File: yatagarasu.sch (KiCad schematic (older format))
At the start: 74 parts, among them CON1 CONSOLE, P1 CONN_02X20, P2 +12V_IN, P3 ttyAMA2, Q1 MMBT3904, Q2 MMBT3904, SW1 RESET, U1 8T245, U16 FT230XS, U17 NCP1117ST18T3G, U18 NCP1117ST33T3G, U19 NCP1117ST50T3G, U2 8T245, U3 PCA9306, U4 PCA9306

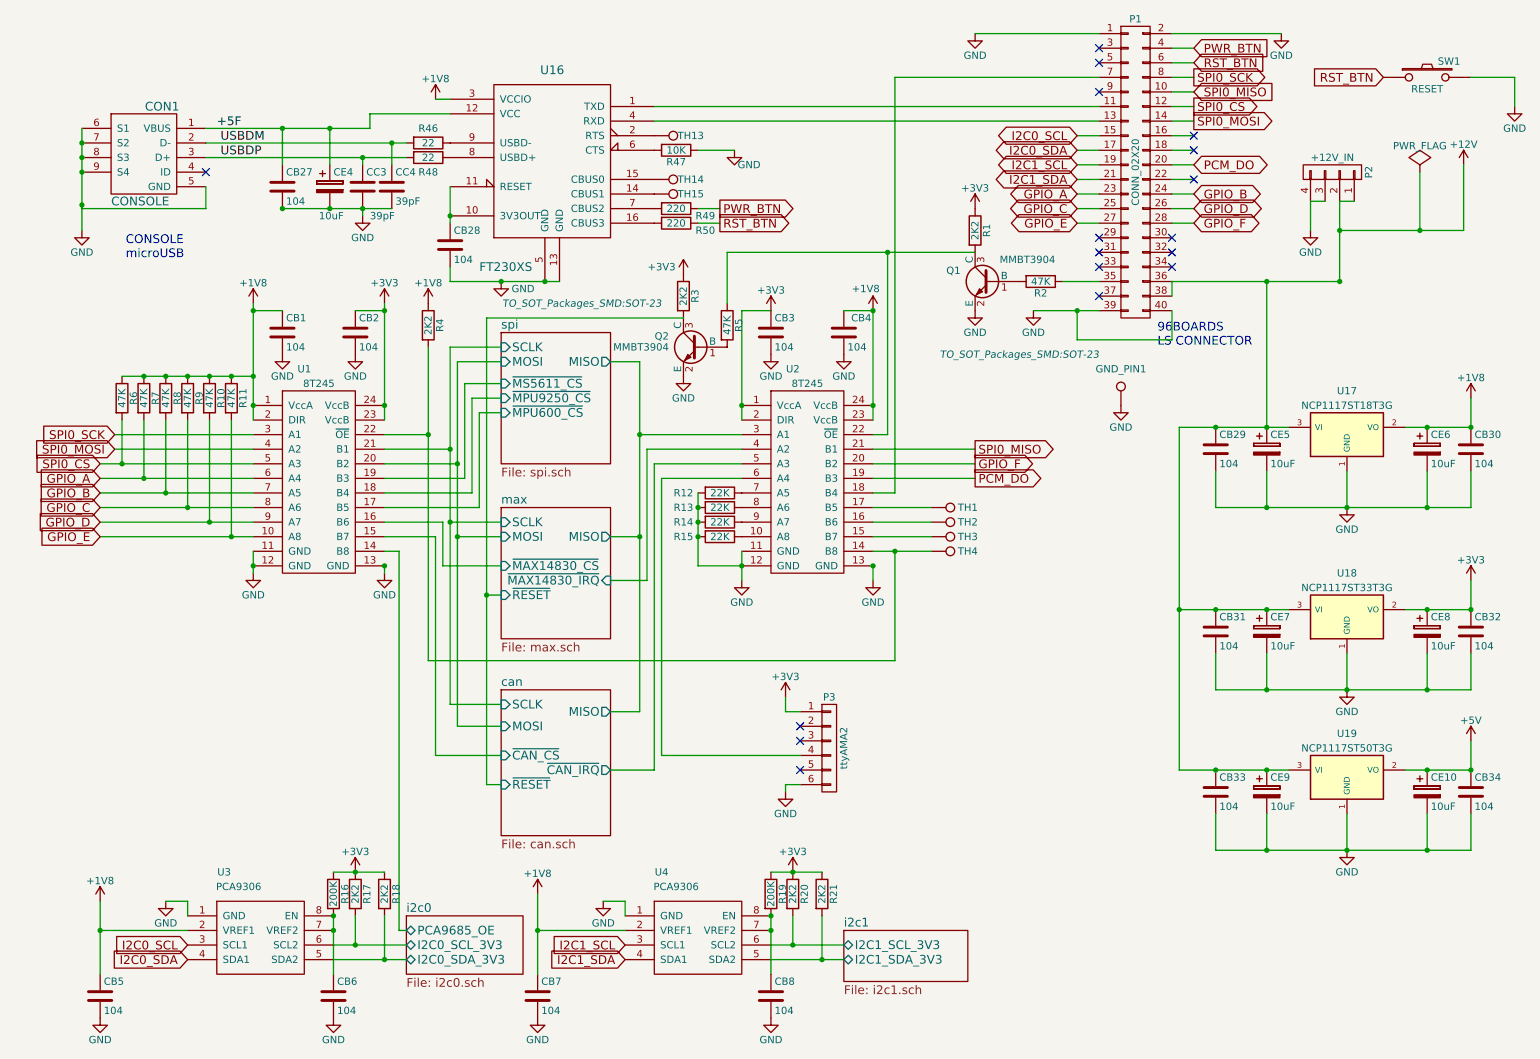
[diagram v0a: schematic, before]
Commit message: Deleted unnecessary files and splitting schmatics.
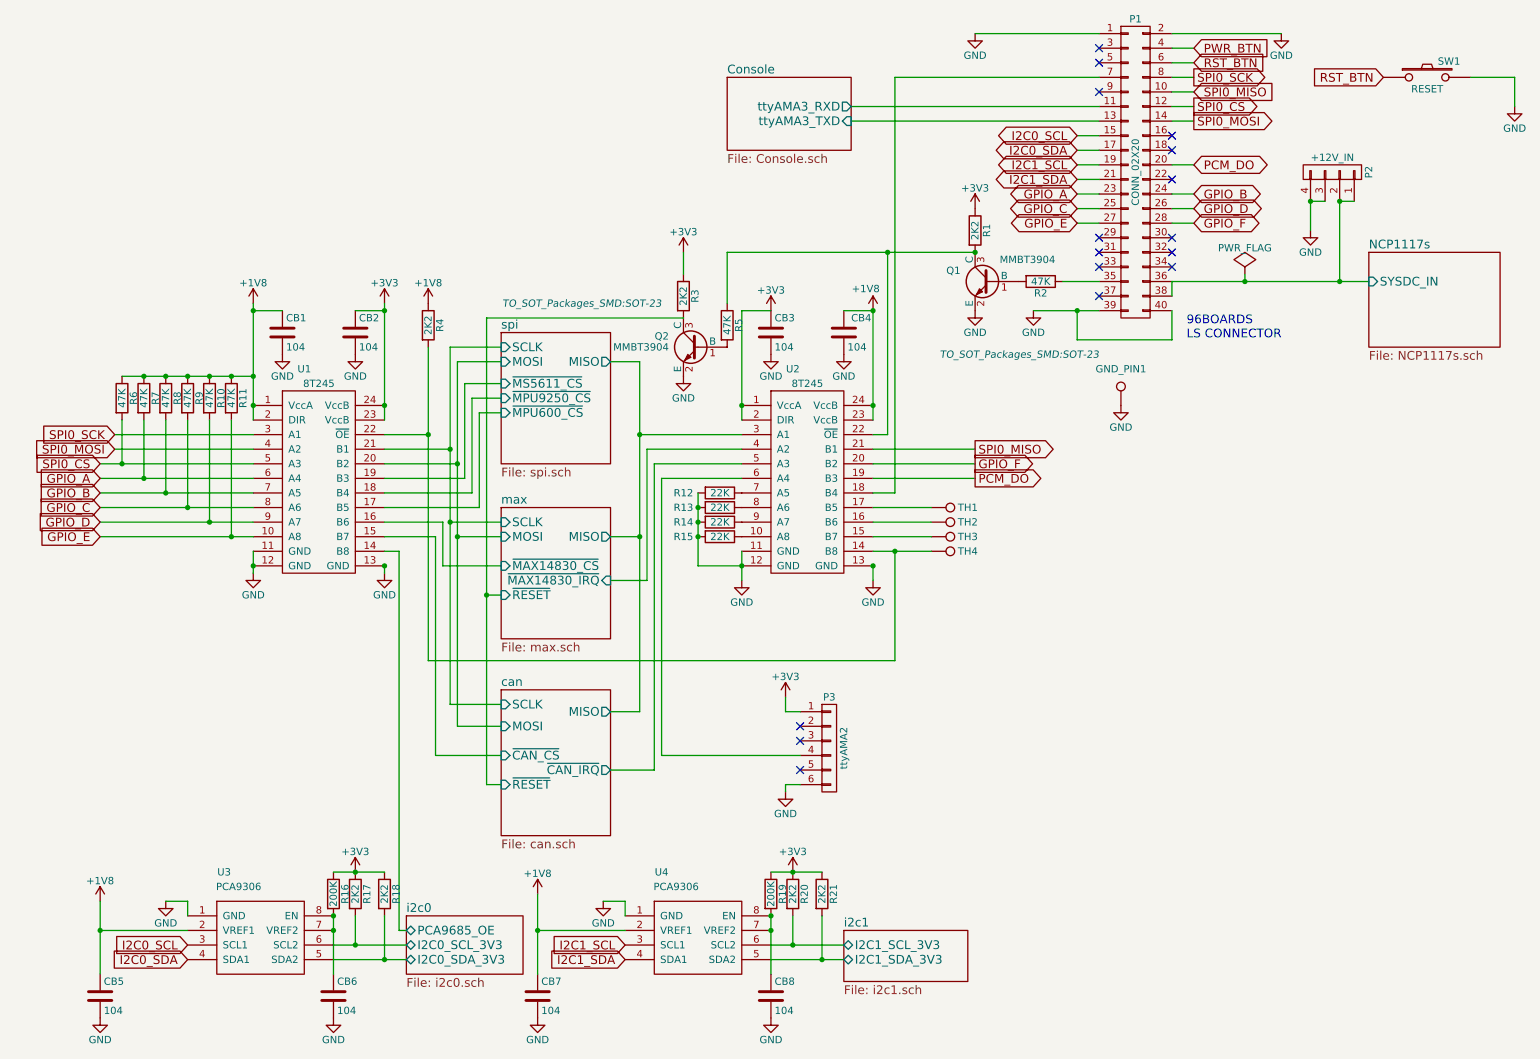
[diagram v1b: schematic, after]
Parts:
- removed CB27, CB28: 104, Capacitors_SMD:C_0603, symbol C
- removed CB29, CB30, CB31, CB32, CB33, CB34: 104, Capacitors_SMD:C_0603_HandSoldering, symbol C
- removed CC3, CC4: 39pF, Capacitors_SMD:C_0603, symbol C
- removed CE10, CE4, CE5, CE6, CE7, CE8, CE9: 10uF, mylib:os-con-A5, symbol CP
- removed CON1: CONSOLE, Sensors:USB_MICRO_B_ST-USB-001E, symbol microUSB-B
- removed R46, R48: 22, Resistors_SMD:R_0603_HandSoldering, symbol R
- removed R47: 10K, Resistors_SMD:R_0603_HandSoldering, symbol R
- removed R49, R50: 220, Resistors_SMD:R_0603_HandSoldering, symbol R
- removed TH13, TH14, TH15: TH, Pin_Headers:Pin_Header_Straight_1x01, symbol TEST_1P
- removed U16: FT230XS, Housings_SSOP:SSOP-16_3.9x4.9mm_Pitch0.635mm, symbol FT230XS
- removed U17: NCP1117ST18T3G, TO_SOT_Packages_SMD:SOT-223, symbol NCP1117ST18T3G
- removed U18: NCP1117ST33T3G, TO_SOT_Packages_SMD:SOT-223, symbol NCP1117ST33T3G
- removed U19: NCP1117ST50T3G, TO_SOT_Packages_SMD:SOT-223, symbol NCP1117ST50T3G
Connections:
- net Console/ttyAMA3_RXD: now reaches P1.11 (P11)
- net Console/ttyAMA3_TXD: now reaches P1.13 (P13)
- net +12V renamed NCP1117s/SYSDC_IN
- no-connect marks 17 -> 16
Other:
- note removed: "CONSOLE \nmicroUSB"
